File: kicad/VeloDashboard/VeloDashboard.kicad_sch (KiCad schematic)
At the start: 53 parts, among them IC1 LDD-700L, IC2 LDD-700L, IC3 LDD-700L, IC4 LDD-700L, J1 Speed Sensor, J1.out Polulu Power, J2 OLED 128 x 64, J3 RJ32, J4 RJ32, K1 HF3-03, Q1 IRF520, Q2 BC546, SW1 On / Off switch, SW2 Down (lights), SW3 Left, SW4 Up (lights), SW5 Horn, SW6 Display, SW7 Right, SW8 Brake, U1 SN74AHCT125N, U2 LC78_05 2.0

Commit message: dahsboard refacture
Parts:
- removed BZ1: Buzzer, symbol Device:Buzzer
- removed D1: D, symbol Device:D
- removed HORN: ~, symbol Device:Buzzer
- removed J3, J4: RJ32, symbol Connector:RJ32
- removed K1: HF3-03, Relay_SMD:Relay_SPDT_AXICOM_HF3Series_75ohms_Pitch1.27mm, symbol Relay:HF3-03
- removed Q1: IRF520, TO270P460X1020X2008-3P, symbol IRF520:IRF520
- removed Q2: BC546, Package_TO_SOT_THT:TO-92_Inline, symbol Transistor_BJT:BC546
- removed R14: 10k, symbol Device:R
- removed R15: 1k, symbol Device:R
- added J4, J5: Conn_01x08_Pin, symbol Connector:Conn_01x08_Pin
- R11, R19, R8: value 220k -> 100k
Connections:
- net +3.3V: now also J5.7 (Pin_7)
- net GND: now also SW2.2, SW3.2, SW4.2, SW5.2, SW6.2, SW7.2, SW8.2, J5.8 (Pin_8); no longer R11.2, R19.2, R8.1
- net at U?.25 (18_A4_SDA0): now also R11.1
- net at U?.26 (19_A5_SCL0): now also R19.1
- net at U?.27 (20_A6_TX5_LRCLK1): now also R8.2
- net at U?.28 (21_A7_RX5_BCLK1): now also R17.1
- net at U?.29 (22_A8_CTX1): now also R16.1
- net at U?.30 (23_A9_CRX1_MCLK1): now also R7.1
- net at J2.1 (Pin_1), U?.31 (3V3): now also J4.7 (Pin_7)
- net at J2.2 (Pin_2), U?.32 (GND): now also J4.8 (Pin_8)
- net at D2.1 (K): now also J5.6 (Pin_6); no longer R7.2
- net at R20.1, SW7.1: now also R13.2, J5.1 (Pin_1); no longer SW5.1, SW6.1
- net at R12.2, R13.1: now also SW6.1; no longer SW6.2
- net at R21.1, SW3.1: now also R9.1, J5.3 (Pin_3); no longer SW2.1, SW4.1
- net at R10.2: now also SW4.1; no longer SW4.2
- net at R10.1, R9.2: now also SW2.1; no longer SW2.2
- net at R18.1, SW8.1: now also J5.2 (Pin_2)
- net at R17.2: now also J4.4 (Pin_4); no longer D4.1 (K)
- net at D3.1 (K): now also J5.5 (Pin_5); no longer R16.2
- new net: R12.1, SW5.1
- new net: J4.6 (Pin_6), R7.2
- new net: J4.2 (Pin_2), R19.2
- new net: J4.1 (Pin_1), R11.2
- new net: J4.3 (Pin_3), R8.1
- new net: J4.5 (Pin_5), R16.2
- new net: D4.1 (K), J5.4 (Pin_4)
- no-connect marks 36 -> 38
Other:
- moved on the sheet: BT1, C1, D2, D3, D4, IC1, IC2, IC3, IC4, J1, J1.in, J1.out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

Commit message: Refacture schema
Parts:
- removed D4: BRAKE, symbol Device:LED
- removed R17: 220, symbol Device:R
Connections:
- net +3.3V: now also J2.1 (Pin_1), U?.31 (3V3); no longer J5.7 (Pin_7)
- net GND: now also J2.2 (Pin_2)
- net Power meter: now also U?.9 (7_RX2_OUT1A)
- net at U?.23 (16_A2_RX4_SCL1): now also J2.3 (Pin_3); no longer J2.4 (Pin_4)
- net at U?.24 (17_A3_TX4_SDA1): now also J2.4 (Pin_4); no longer J2.3 (Pin_3)
- net at J4.8 (Pin_8), U?.32 (GND): no longer J2.2 (Pin_2)
- net at J5.1 (Pin_1), R13.2, SW7.1: no longer R20.1
- net at J4.2 (Pin_2), R19.2: now also R18.1
- net at J5.2 (Pin_2), SW8.1: no longer R18.1
- net at J5.3 (Pin_3), R9.1, SW3.1: no longer R21.1
- net at J4.1 (Pin_1), R11.2: now also R21.1
- net at J4.3 (Pin_3), R8.1: now also R20.1
- now unconnected: J4.7 (Pin_7)
- no-connect marks 38 -> 43
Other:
- note added: "Dashboard"
- moved on the sheet: BT1, D2, D3, IC1, IC2, IC3, IC4, J1, J2, J4, J5, R1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

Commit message: update pcb
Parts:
- gave numbers to parts that had none: 1
- renumbered D2 to D1, D3 to D2, J2 to J1, J1.in to J1.in1, J1.out to J1.out1, J1 to J2, J4 to J3, J5 to J4, R5 to R1, R7 to R10, R9 to R11, R10 to R12, R1 to R13, R2 to R14, R3 to R15, R4 to R16, R12 to R17, R13 to R18, R6 to R2, R8 to R3, R19 to R4, R11 to R5, R21 to R6, R18 to R7, R20 to R8, R16 to R9, SW3 to SW2, SW2 to SW3, SW8 to SW5, SW5 to SW6, SW6 to SW7, SW7 to SW8
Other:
- moved on the sheet: IC1, IC2, IC3, IC4, J3, R10, R13, R14, R15, R16, R3, R4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

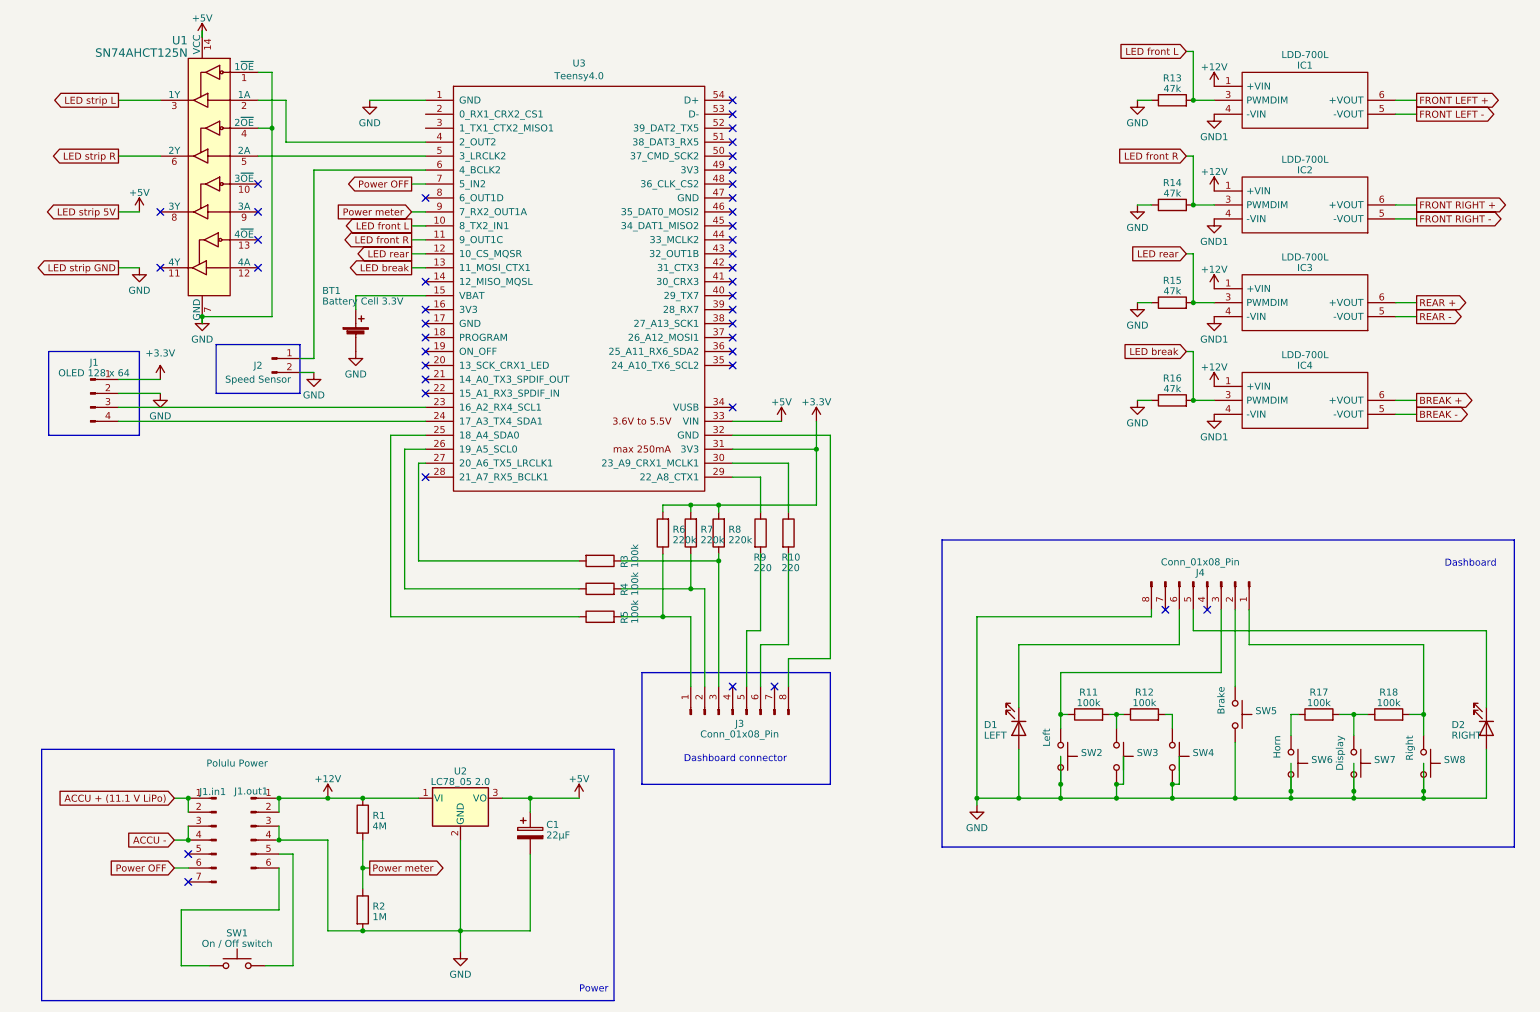
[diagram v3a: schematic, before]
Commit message: added blinker drivers
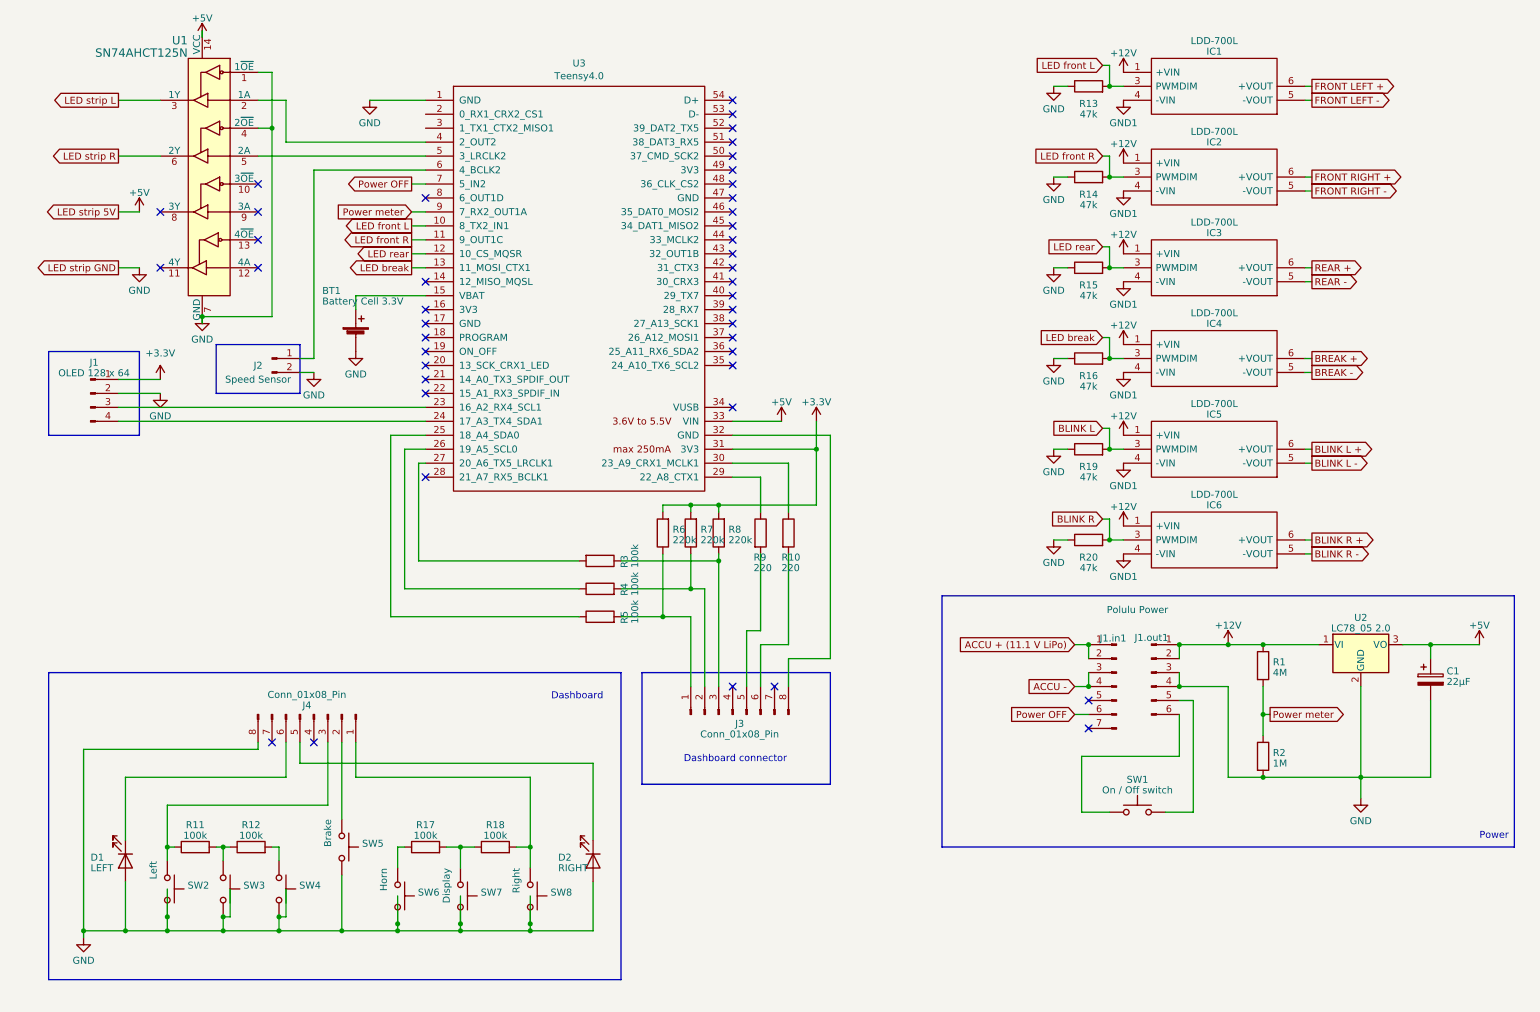
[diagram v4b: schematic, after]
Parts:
- added IC5, IC6: LDD-700L, LDD-XXXL, symbol LDD-700L:LDD-700L
- added R19, R20: 47k, symbol Device:R
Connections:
- net +12V: now also IC5.1 (+VIN), IC6.1 (+VIN)
- net GND: now also R19.1, R20.1
- net GND1: now also IC5.4 (-VIN), IC6.4 (-VIN)
- new net BLINK L: IC5.3 (PWMDIM), R19.2
- new net BLINK L +: IC5.6 (+VOUT)
- new net BLINK L -: IC5.5 (-VOUT)
- new net BLINK R: IC6.3 (PWMDIM), R20.2
- new net BLINK R +: IC6.6 (+VOUT)
- new net BLINK R -: IC6.5 (-VOUT)
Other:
- moved on the sheet: C1, D1, D2, IC1, IC2, IC3, IC4, J1.in1, J1.out1, J4, R1, R11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
